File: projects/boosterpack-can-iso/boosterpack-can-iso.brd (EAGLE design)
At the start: 63.5 x 34.3 mm, 4 parts

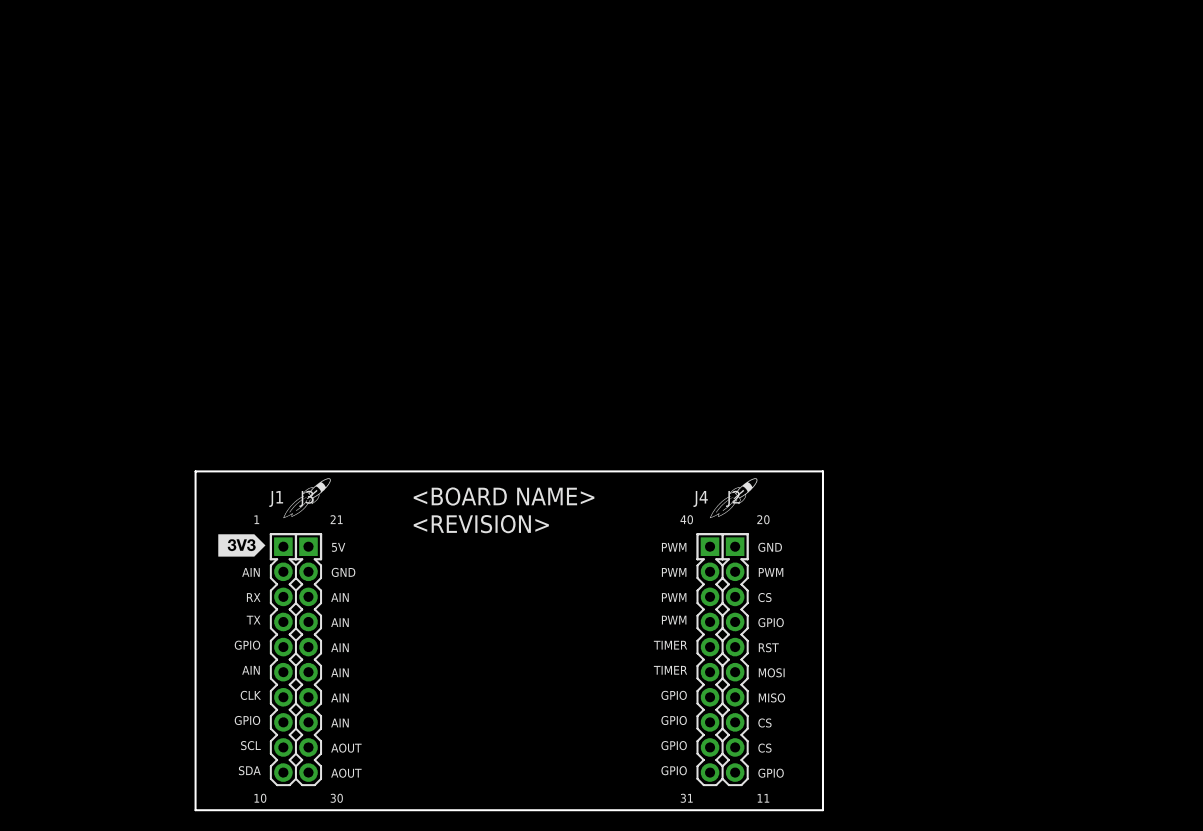
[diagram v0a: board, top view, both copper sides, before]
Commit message: Added markdown documentation files.
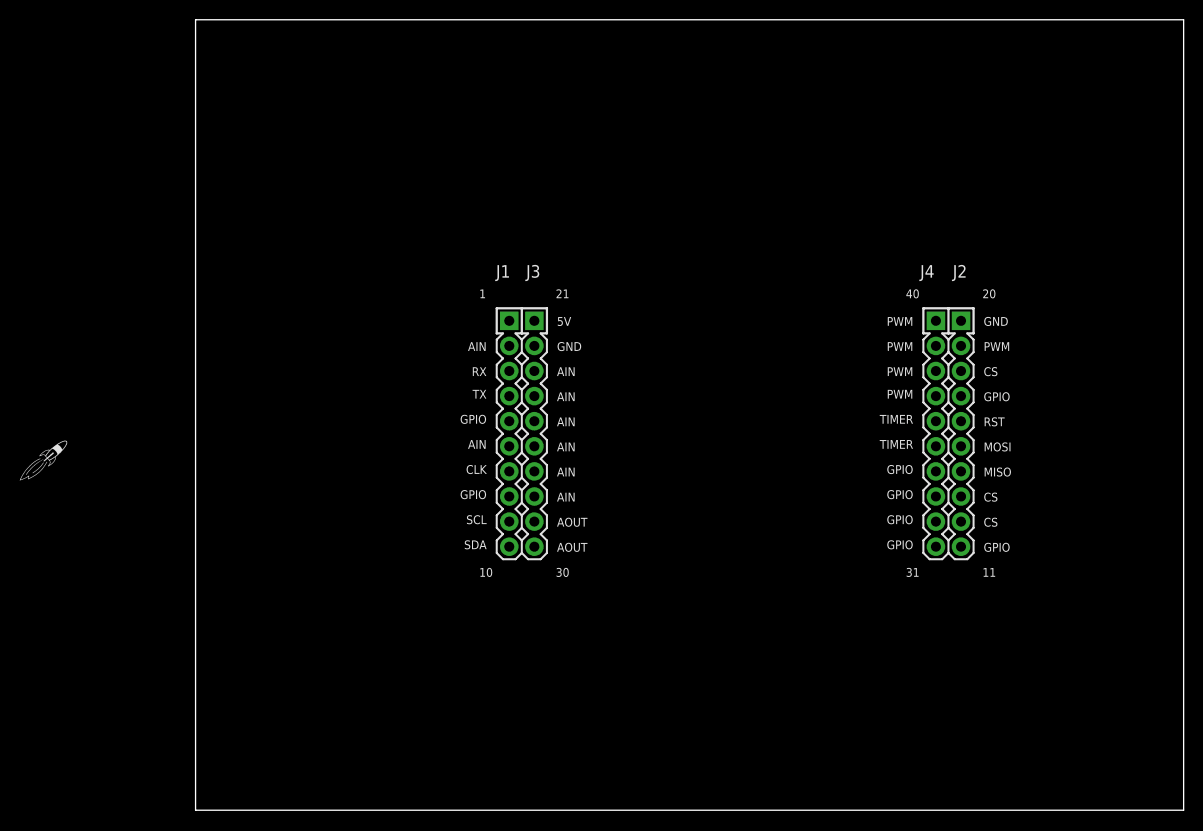
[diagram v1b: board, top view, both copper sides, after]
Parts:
- removed U$2: (no value), CCo-Boost:LOGO-ROCKET
- removed U$3: SILK_3V3_TAG, Public_BP_Library:SILK_3V3_TAG
- added FRAME1: FRAME-LETTERNO_PACKAGE, SparkFun-Aesthetics:DUMMY
- A1: device Public_BP_Library:4X10-BOOSTERPACK -> EAGLE_BoosterPack_Library:4X10-BOOSTERPACK
- U$1: value (none) -> LOGO-ROCKET; device CCo-Boost:LOGO-ROCKET -> EAGLE_BoosterPack_Library:LOGO-ROCKET
- moved U$1 70.0 mm to (-15.2, 35.6)
- moved A1 32.3 mm to (31.8, 39.4)
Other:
- board size 63.5 x 34.3 mm -> 100 x 80 mm
- board text removed: "<BOARD NAME>"
- board text removed: "<REVISION>"
